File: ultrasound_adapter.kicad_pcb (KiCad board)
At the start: 2 copper layers, 18.1 x 20.1 mm, 3 parts, among them J1 Conn_01x04, J2 Conn_01x04

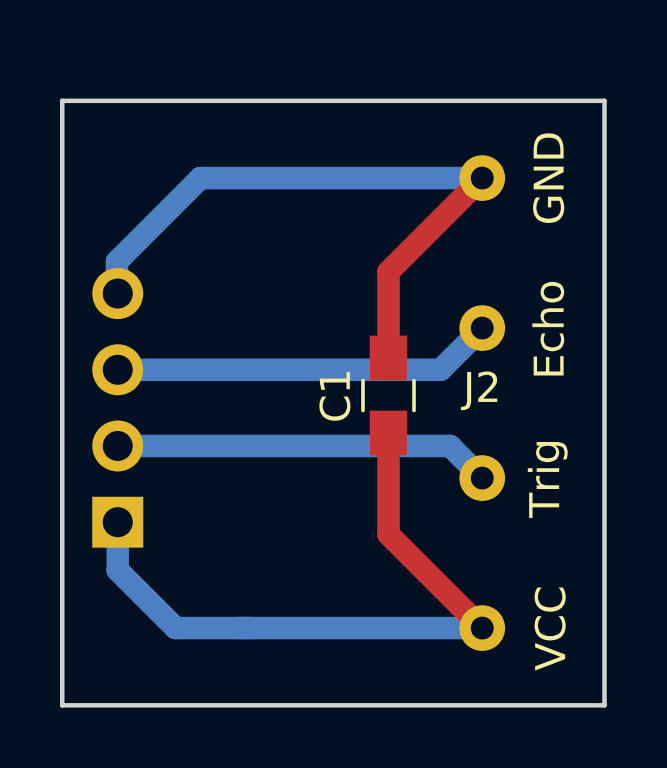
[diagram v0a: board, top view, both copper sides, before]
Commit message: Added mounting holes and changed capacitor to be a large Electrolytic
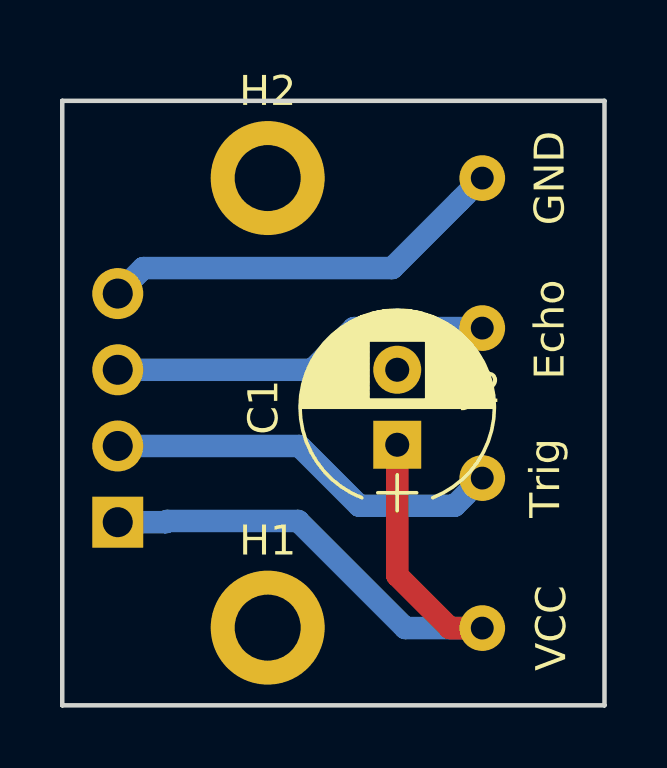
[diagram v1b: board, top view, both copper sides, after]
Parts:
- added H1: MountingHole, Mounting_Holes:MountingHole_2.2mm_M2_DIN965_Pad, F.Cu at (130.0, 61.0)
- added H2: MountingHole, Mounting_Holes:MountingHole_2.2mm_M2_DIN965_Pad, F.Cu at (130.0, 46.0)
- C1: value C -> CP; footprint Capacitors_SMD:C_0805_HandSoldering -> Capacitors_THT:CP_Radial_D6.3mm_P2.50mm
- moved C1 1.66 mm to (134.4, 54.9)
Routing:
- net VCC: track 40.6 -> 21.6 mm
- net GND: track 29.0 -> 13.7 mm
- net Echo: track 25.5 -> 12.7 mm
- net Trig: track 25.2 -> 13.4 mm

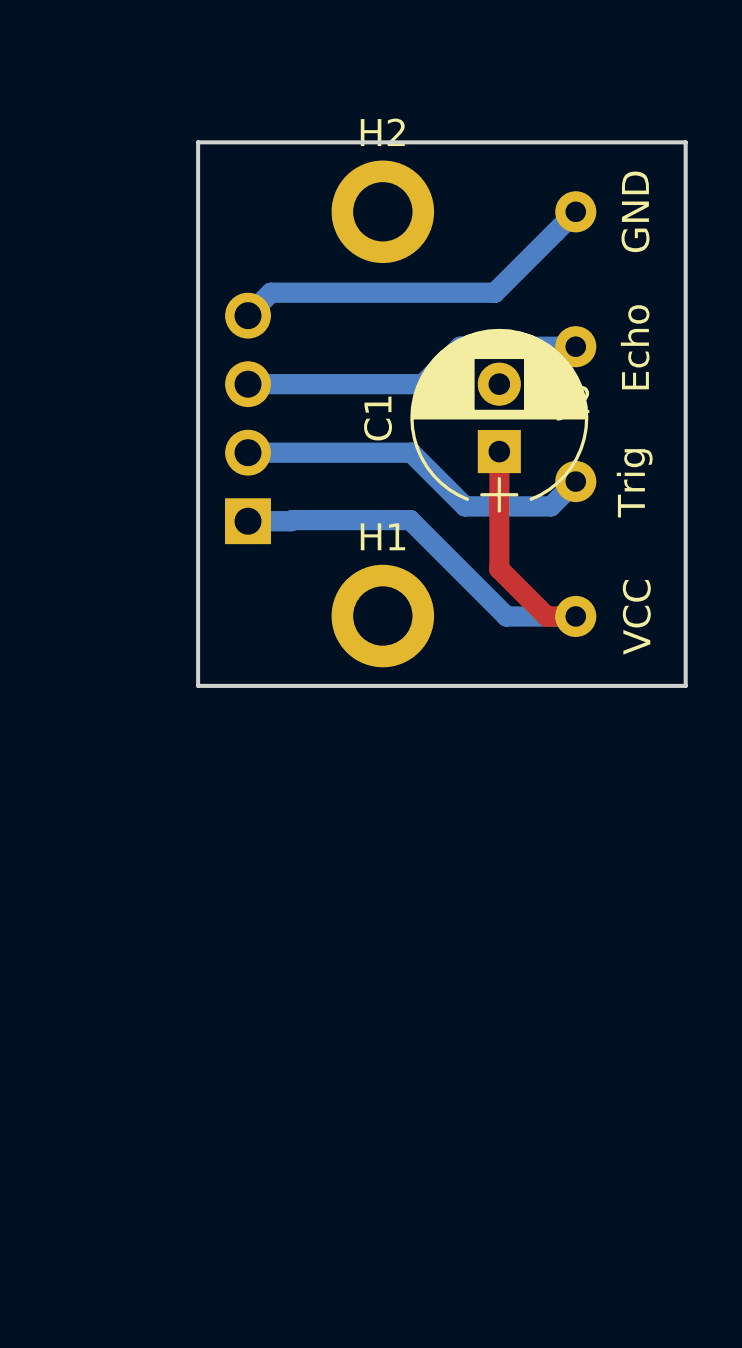
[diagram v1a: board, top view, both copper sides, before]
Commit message: size increased, mounting holes made to be M3, layout changed
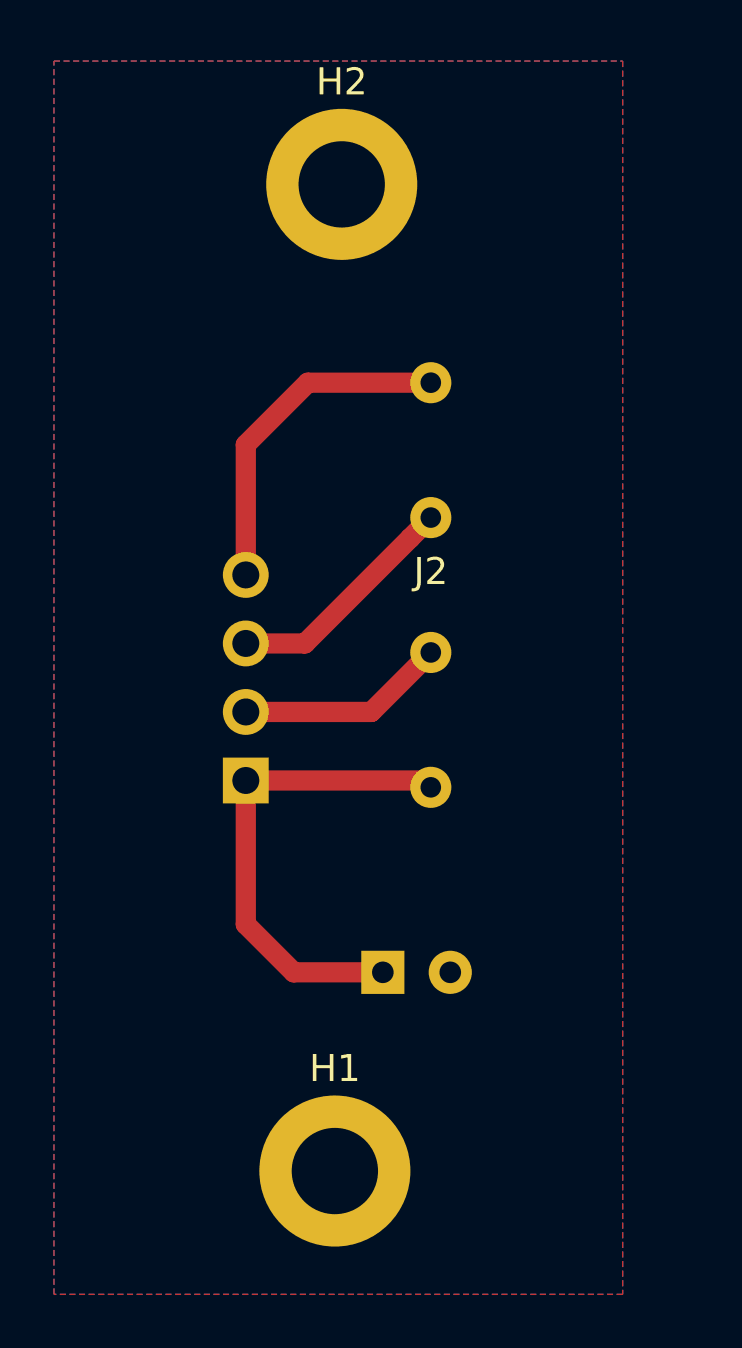
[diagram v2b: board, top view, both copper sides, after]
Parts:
- C1: moved to B.Cu
- H1, H2: footprint Mounting_Holes:MountingHole_2.2mm_M2_DIN965_Pad -> Mounting_Holes:MountingHole_3.2mm_M3_DIN965_Pad
- moved H1 20.7 mm to (128.3, 81.5)
- moved C1 19.8 mm to (130.0, 74.2), turned to 0 degrees
- moved J1 9.61 mm to (125.0, 67.1)
- moved J2 8.31 mm to (131.8, 59.8)
- moved H2 1.83 mm to (128.5, 45.0)
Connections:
- H1 pad 1: GND -> (no net)
- H2 pad 1: GND -> (no net)
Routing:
- net Trig: track 13.4 -> 7.77 mm
- net Echo: track 12.7 -> 8.79 mm
- net VCC: track 21.6 -> 18.1 mm
- net GND: track 13.7 -> 12.6 mm
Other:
- board outline removed

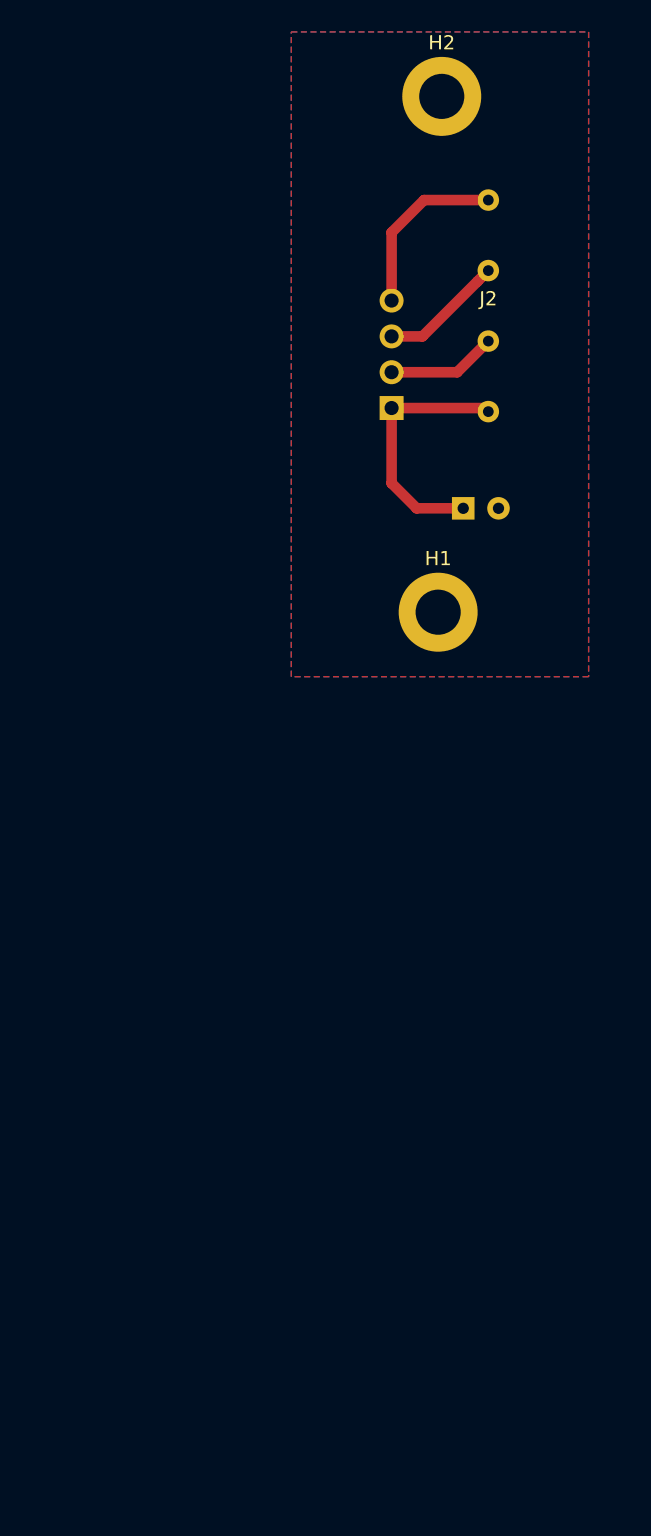
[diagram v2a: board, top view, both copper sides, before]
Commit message: Updated board to add outline.
Also added readme
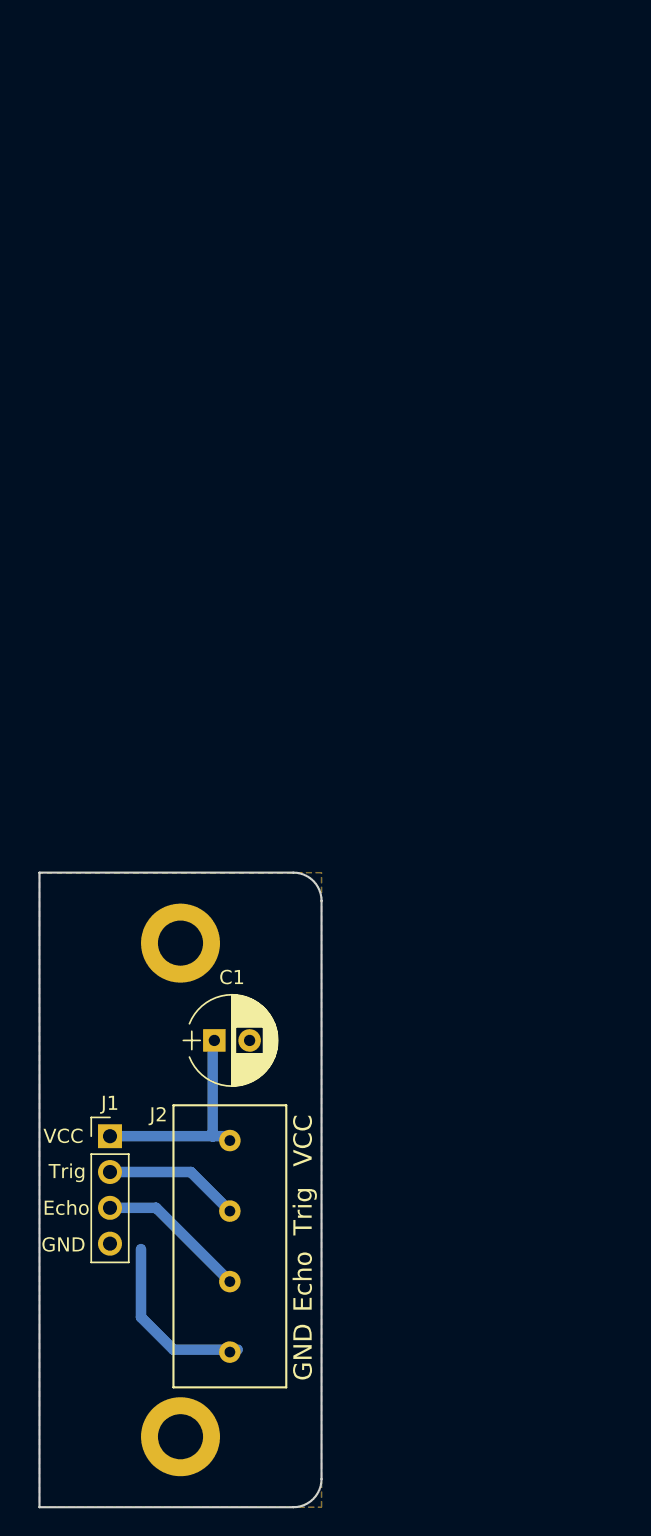
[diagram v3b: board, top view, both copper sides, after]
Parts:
- C1, J1, J2: moved to F.Cu
- H1, H2: moved to B.Cu
- moved H2 96.8 mm to (110.0, 140.0)
- moved J2 69.2 mm to (113.5, 126.5)
- moved J1 55.4 mm to (105.0, 118.7)
- moved C1 41.7 mm to (112.4, 111.9)
- moved H1 29.7 mm to (110.0, 105.0)
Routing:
- net VCC: track 18.1 -> 15.4 mm
- net Echo: track 8.79 -> 10.7 mm
- net Trig: track 7.77 -> 9.65 mm
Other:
- board outline added: 20 x 45 mm

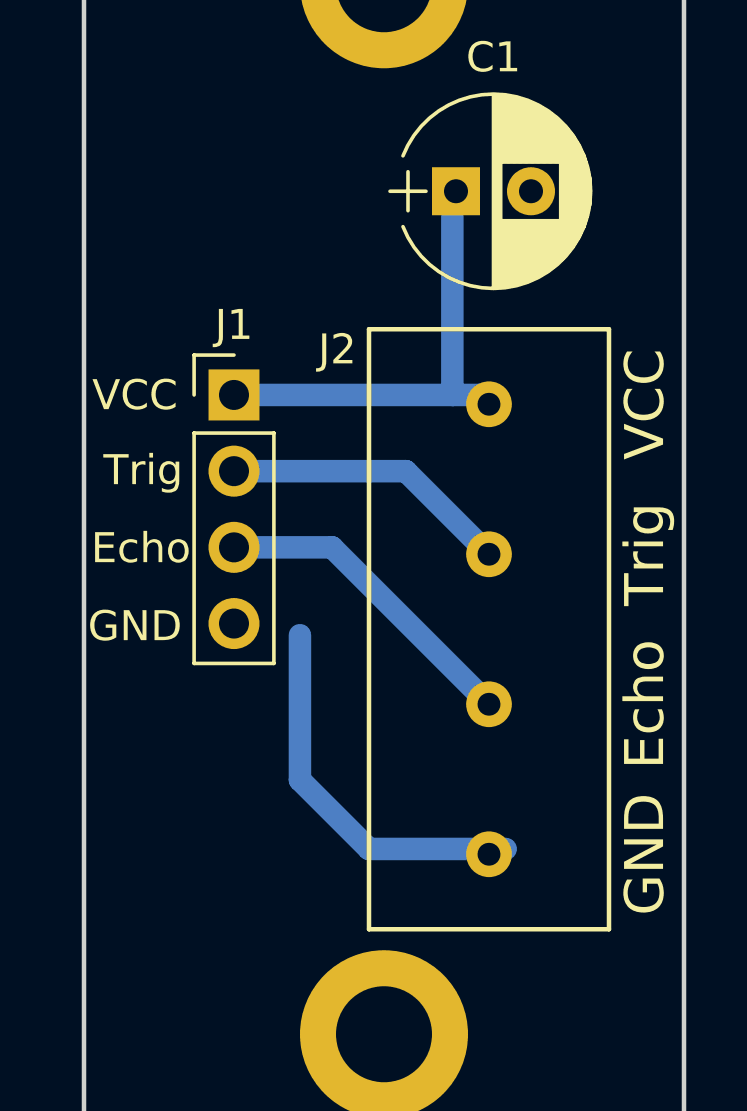
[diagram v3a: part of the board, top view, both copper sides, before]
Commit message: Moved screw terminal back as it is larger than the silkscreen
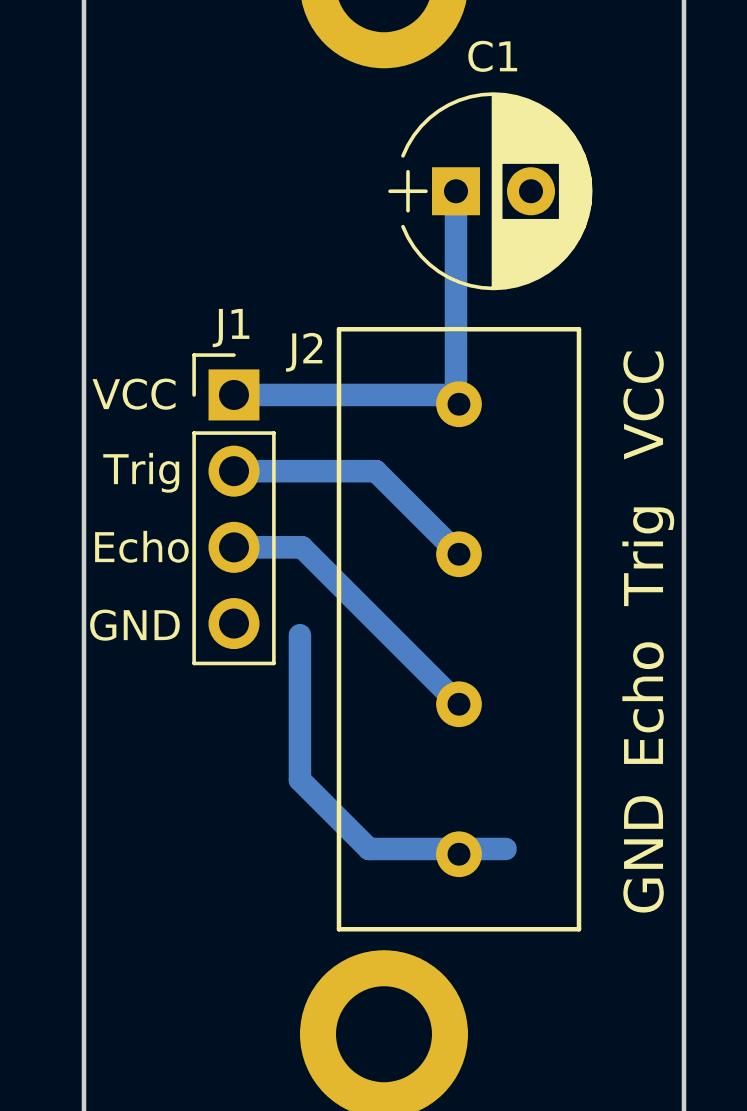
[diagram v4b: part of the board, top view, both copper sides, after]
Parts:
- moved J2 1.00 mm to (112.5, 126.5)
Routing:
- net Trig: track 9.65 -> 8.65 mm
- net Echo: track 10.7 -> 9.67 mm
- net VCC: track 15.4 -> 14.8 mm
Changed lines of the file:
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@@
     (add_net VCC)
+  )
+  (module 4Way_Screw_terminal:Screw_terminals (layer F.Cu)
+    (at 112.5 126.5)
+    (fp_text reference J2 (at -5.056 -9.324) (layer F.SilkS)
+      (effects (font (size 1 1) (thickness 0.15)))
+    )
+    (fp_text value Conn_01x04 (at 0 -0.5) (layer F.Fab)
+      (effects (font (size 1 1) (thickness 0.15)))
+    )
+    (fp_line (start -4 -10) (end -4 10) (layer F.SilkS) (width 0.15))
+    (fp_line (start 4 -10) (end -4 -10) (layer F.SilkS) (width 0.15))
+    (fp_line (start 4 10) (end 4 -10) (layer F.SilkS) (width 0.15))
+    (fp_line (start -4 10) (end 4 10) (layer F.SilkS) (width 0.15))
+    (pad 4 thru_hole circle (at 0 7.5) (size 1.524 1.524) (drill 0.762) (layers *.Cu *.Mask)
+      (net 1 GND))
+    (pad 3 thru_hole circle (at 0 2.5) (size 1.524 1.524) (drill 0.762) (layers *.Cu *.Mask)
+      (net 3 Echo))
+    (pad 2 thru_hole circle (at 0 -2.5) (size 1.524 1.524) (drill 0.762) (layers *.Cu *.Mask)
+      (net 4 Trig))
+    (pad 1 thru_hole circle (at 0 -7.5) (size 1.524 1.524) (drill 0.762) (layers *.Cu *.Mask)
+      (net 2 VCC))
   )
   (module Capacitors_THT:CP_Radial_D6.3mm_P2.50mm (layer F.Cu)
@@
     )
   )
-  (module 4Way_Screw_terminal:Screw_terminals (layer F.Cu)
-    (at 113.5 126.5)
-    (fp_text reference J2 (at -5.056 -9.324) (layer F.SilkS)
-      (effects (font (size 1 1) (thickness 0.15)))
-    )
-    (fp_text value Conn_01x04 (at 0 -0.5) (layer F.Fab)
-      (effects (font (size 1 1) (thickness 0.15)))
-    )
-    (fp_line (start -4 -10) (end -4 10) (layer F.SilkS) (width 0.15))
-    (fp_line (start 4 -10) (end -4 -10) (layer F.SilkS) (width 0.15))
-    (fp_line (start 4 10) (end 4 -10) (layer F.SilkS) (width 0.15))
-    (fp_line (start -4 10) (end 4 10) (layer F.SilkS) (width 0.15))
-    (pad 4 thru_hole circle (at 0 7.5) (size 1.524 1.524) (drill 0.762) (layers *.Cu *.Mask)
-      (net 1 GND))
-    (pad 3 thru_hole circle (at 0 2.5) (size 1.524 1.524) (drill 0.762) (layers *.Cu *.Mask)
-      (net 3 Echo))
-    (pad 2 thru_hole circle (at 0 -2.5) (size 1.524 1.524) (drill 0.762) (layers *.Cu *.Mask)
-      (net 4 Trig))
-    (pad 1 thru_hole circle (at 0 -7.5) (size 1.524 1.524) (drill 0.762) (layers *.Cu *.Mask)
-      (net 2 VCC))
-  )
   (module Mounting_Holes:MountingHole_3.2mm_M3_DIN965_Pad (layer B.Cu)
     (at 110 105)
@@
   (segment (start 107.198 126.698) (end 107.198 131.524) (width 0.75) (layer B.Cu) (net 1))
   (segment (start 107.198 131.524) (end 109.498 133.824) (width 0.75) (layer B.Cu) (net 1))
-  (segment (start 113.19 118.69) (end 113.5 119) (width 0.75) (layer B.Cu) (net 2))
   (segment (start 112.278 118.678) (end 112.29 118.69) (width 0.75) (layer B.Cu) (net 2))
-  (segment (start 112.278 111.966) (end 112.278 118.678) (width 0.75) (layer B.Cu) (net 2))
-  (segment (start 105 118.69) (end 112.29 118.69) (width 0.75) (layer B.Cu) (net 2))
-  (segment (start 112.29 118.69) (end 113.19 118.69) (width 0.75) (layer B.Cu) (net 2))
-  (segment (start 108.27 123.77) (end 113.5 129) (width 0.75) (layer B.Cu) (net 3))
-  (segment (start 105 123.77) (end 108.27 123.77) (width 0.75) (layer B.Cu) (net 3))
-  (segment (start 110.73 121.23) (end 113.5 124) (width 0.75) (layer B.Cu) (net 4))
-  (segment (start 105 121.23) (end 110.73 121.23) (width 0.75) (layer B.Cu) (net 4))
+  (segment (start 112.19 118.69) (end 112.5 119) (width 0.75) (layer B.Cu) (net 2))
+  (segment (start 105 118.69) (end 112.19 118.69) (width 0.75) (layer B.Cu) (net 2))
+  (segment (start 112.4 118.9) (end 112.5 119) (width 0.75) (layer B.Cu) (net 2))
+  (segment (start 112.4 111.9) (end 112.4 118.9) (width 0.75) (layer B.Cu) (net 2))
+  (segment (start 107.27 123.77) (end 112.5 129) (width 0.75) (layer B.Cu) (net 3))
+  (segment (start 105 123.77) (end 107.27 123.77) (width 0.75) (layer B.Cu) (net 3))
+  (segment (start 109.73 121.23) (end 112.5 124) (width 0.75) (layer B.Cu) (net 4))
+  (segment (start 105 121.23) (end 109.73 121.23) (width 0.75) (layer B.Cu) (net 4))
   (zone (net 1) (net_name GND) (layer B.Cu) (hatch edge 0.508)
     (connect_pads (clearance 0.508))

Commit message: Added revision info to board
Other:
- board text added: "Ultrasound adapter"
- board text added: "r1.0"
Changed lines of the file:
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@@
   (general
     (thickness 1.6)
-    (drawings 14)
+    (drawings 16)
     (tracks 12)
     (zones 0)
@@
       (drillshape 0)
       (scaleselection 1)
-      (outputdirectory ""))
+      (outputdirectory "gerbers/r1.0/"))
   )
   (net 0 "")
@@
     (pad 1 thru_hole circle (at 0 0) (size 5.6 5.6) (drill 3.2) (layers *.Cu *.Mask))
   )
+  (gr_text "Ultrasound adapter" (at 107.9 143.9) (layer F.Mask)
+    (effects (font (size 1 1) (thickness 0.15)))
+  )
+  (gr_text r1.0 (at 103.8 141.8) (layer F.Mask)
+    (effects (font (size 2 2) (thickness 0.4)))
+  )
   (gr_arc (start 118 143) (end 118 145) (angle -90) (layer Edge.Cuts) (width 0.15))
